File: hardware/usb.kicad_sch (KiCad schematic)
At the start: 7 parts, among them J201 USB_C_Receptacle_USB2.0, U201 SRV05-4

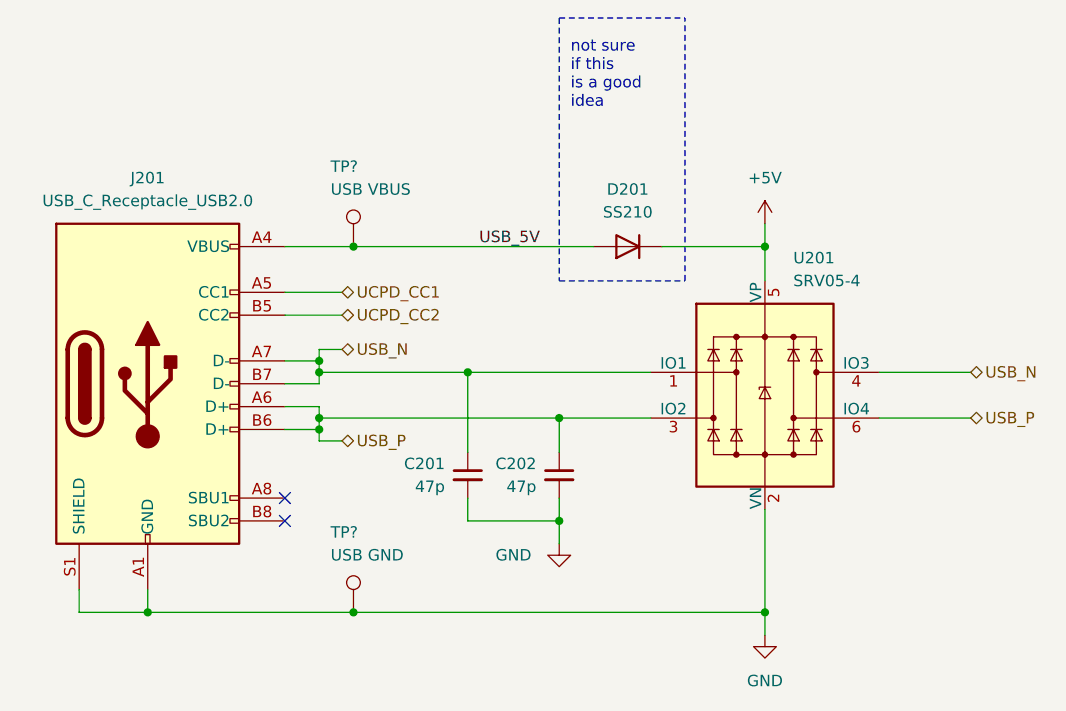
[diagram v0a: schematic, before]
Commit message: finish component selection
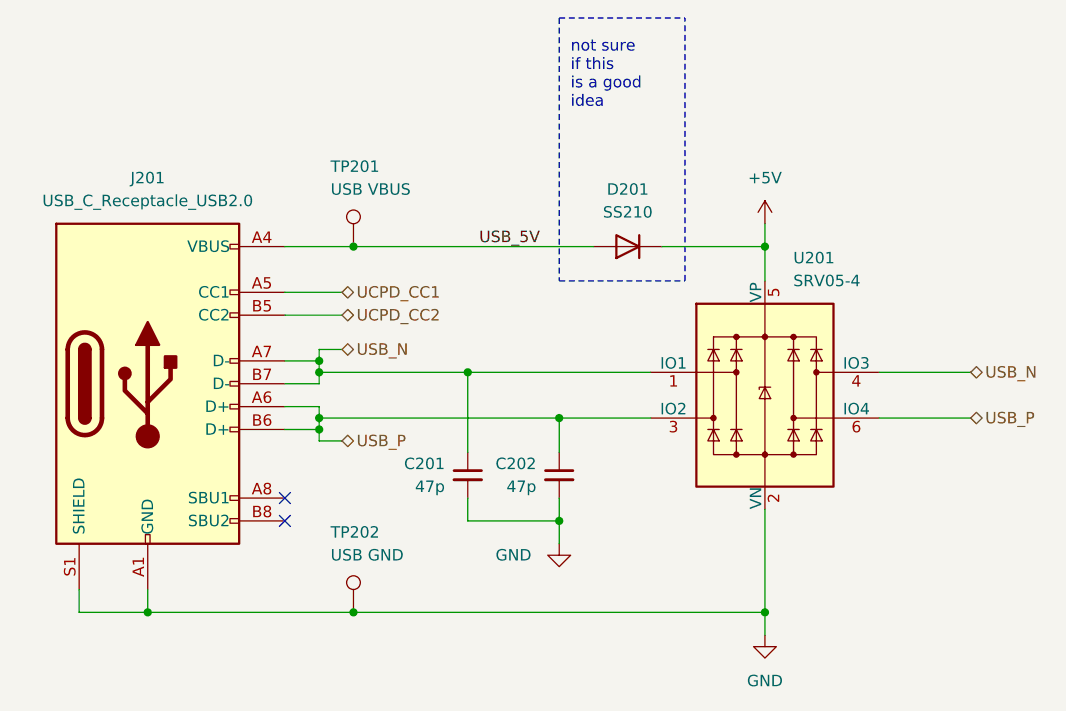
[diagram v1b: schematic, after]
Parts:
- J201: footprint Connector_USB:USB_C_Receptacle_HRO_TYPE-C-31-M-12 -> easyeda2kicad:USB-C-SMD_GT-USB-7052_1; LCSC Part (none) -> C963223
- gave numbers to parts that had none: 2
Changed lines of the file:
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@@
   (title_block
     (title "USB & ESD")
-    (date "2023-06-17")
-    (rev "1.0")
+    (date "2023-10-11")
+    (rev "0.1")
     (company "matei repair lab")
   )
@@
   (symbol (lib_id "Connector:TestPoint") (at 137.16 115.57 0) (unit 1)
     (in_bom yes) (on_board yes) (dnp no)
-    (property "Reference" "TP?" (at 134.62 106.68 0)
+    (property "Reference" "TP202" (at 134.62 106.68 0)
       (effects (font (size 1.27 1.27)) (justify left))
     )
@@
     (pin "1")
     (instances
-      (project "sfoc-stepper"
-        (path "/0306e2fa-4433-4288-91d9-65a3484207ad/3af4e77c-61b4-4c93-bd22-ce60f55b568c"
-          (reference "TP?") (unit 1)
+      (project "lemon-pepper"
+        (path "/0306e2fa-4433-4288-91d9-65a3484207ad/3af4e77c-61b4-4c93-bd22-ce60f55b568c"
+          (reference "TP202") (unit 1)
         )
       )
@@
     (pin "6")
     (instances
-      (project "sfoc-stepper"
+      (project "lemon-pepper"
         (path "/0306e2fa-4433-4288-91d9-65a3484207ad/3af4e77c-61b4-4c93-bd22-ce60f55b568c"
           (reference "U201") (unit 1)
@@
   (symbol (lib_id "Connector:TestPoint") (at 137.16 74.93 0) (unit 1)
     (in_bom yes) (on_board yes) (dnp no)
-    (property "Reference" "TP?" (at 134.62 66.04 0)
+    (property "Reference" "TP201" (at 134.62 66.04 0)
       (effects (font (size 1.27 1.27)) (justify left))
     )
@@
     (pin "1")
     (instances
-      (project "sfoc-stepper"
-        (path "/0306e2fa-4433-4288-91d9-65a3484207ad/3af4e77c-61b4-4c93-bd22-ce60f55b568c"
-          (reference "TP?") (unit 1)
+      (project "lemon-pepper"
+        (path "/0306e2fa-4433-4288-91d9-65a3484207ad/3af4e77c-61b4-4c93-bd22-ce60f55b568c"
+          (reference "TP201") (unit 1)
         )
       )
@@
       (effects (font (size 1.27 1.27)))
     )
-    (property "Footprint" "Connector_USB:USB_C_Receptacle_HRO_TYPE-C-31-M-12" (at 118.11 90.17 0)
+    (property "Footprint" "easyeda2kicad:USB-C-SMD_GT-USB-7052_1" (at 118.11 90.17 0)
       (effects (font (size 1.27 1.27)) hide)
     )
     (property "Datasheet" "https://www.usb.org/sites/default/files/documents/usb_type-c.zip" (at 118.11 90.17 0)
+      (effects (font (size 1.27 1.27)) hide)
+    )
+    (property "LCSC Part" "C963223" (at 114.3 90.17 0)
       (effects (font (size 1.27 1.27)) hide)
     )
@@
     (pin "S1")
     (instances
-      (project "sfoc-stepper"
+      (project "lemon-pepper"
         (path "/0306e2fa-4433-4288-91d9-65a3484207ad/3af4e77c-61b4-4c93-bd22-ce60f55b568c"
           (reference "J201") (unit 1)
@@
     (pin "1")
     (instances
-      (project "sfoc-stepper"
+      (project "lemon-pepper"
         (path "/0306e2fa-4433-4288-91d9-65a3484207ad/3af4e77c-61b4-4c93-bd22-ce60f55b568c"
           (reference "#PWR0202") (unit 1)
@@
     (pin "2")
     (instances
-      (project "sfoc-stepper"
+      (project "lemon-pepper"
         (path "/0306e2fa-4433-4288-91d9-65a3484207ad/3af4e77c-61b4-4c93-bd22-ce60f55b568c"
           (reference "D201") (unit 1)
@@
     (pin "2")
     (instances
-      (project "sfoc-stepper"
+      (project "lemon-pepper"
         (path "/0306e2fa-4433-4288-91d9-65a3484207ad/3af4e77c-61b4-4c93-bd22-ce60f55b568c"
           (reference "C202") (unit 1)
@@
     (pin "1")
     (instances
-      (project "sfoc-stepper"
+      (project "lemon-pepper"
         (path "/0306e2fa-4433-4288-91d9-65a3484207ad/3af4e77c-61b4-4c93-bd22-ce60f55b568c"
           (reference "#PWR0201") (unit 1)
@@
     (pin "2")
     (instances
-      (project "sfoc-stepper"
+      (project "lemon-pepper"
         (path "/0306e2fa-4433-4288-91d9-65a3484207ad/3af4e77c-61b4-4c93-bd22-ce60f55b568c"
           (reference "C201") (unit 1)
@@
     (pin "1")
     (instances
-      (project "sfoc-stepper"
+      (project "lemon-pepper"
         (path "/0306e2fa-4433-4288-91d9-65a3484207ad/3af4e77c-61b4-4c93-bd22-ce60f55b568c"
           (reference "#PWR0203") (unit 1)

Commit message: try new driver
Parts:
- D201: value SS210 -> 1N4148WS; footprint Diode_SMD:D_SMA -> Diode_SMD:D_SOD-323; LCSC Part C14996 -> C2128
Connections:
- net USB_5V: now also U201.5 (VP)
- net USB_N: now also U201.3 (IO2); no longer U201.1 (IO1)
- net USB_P: now also U201.1 (IO1); no longer U201.3 (IO2)
- net +5V renamed Vmot
- net Vmot: no longer U201.5 (VP)
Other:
- note removed: "not sure if this is a good idea"

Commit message: finish layout and prod files
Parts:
- removed TP201: USB VBUS, TestPoint:TestPoint_Pad_D1.0mm, symbol Connector:TestPoint
- removed TP202: USB GND, TestPoint:TestPoint_Pad_D1.0mm, symbol Connector:TestPoint
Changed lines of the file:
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@@
   (junction (at 160.02 93.98) (diameter 0) (color 0 0 0 0)
   )
-  (junction (at 137.16 74.93) (diameter 0) (color 0 0 0 0)
-  )
   (junction (at 160.02 105.41) (diameter 0) (color 0 0 0 0)
-  )
-  (junction (at 137.16 115.57) (diameter 0) (color 0 0 0 0)
   )
   (junction (at 149.86 88.9) (diameter 0) (color 0 0 0 0)
@@
     (stroke (width 0) (type default))
   )
-  (wire (pts (xy 129.54 74.93) (xy 137.16 74.93))
+  (wire (pts (xy 129.54 74.93) (xy 182.88 74.93))
     (stroke (width 0) (type default))
   )
@@
     (stroke (width 0) (type default))
   )
-  (wire (pts (xy 137.16 115.57) (xy 182.88 115.57))
-    (stroke (width 0) (type default))
-  )
   (wire (pts (xy 182.88 74.93) (xy 193.04 74.93))
     (stroke (width 0) (type default))
@@
     (stroke (width 0) (type default))
   )
-  (wire (pts (xy 137.16 74.93) (xy 182.88 74.93))
-    (stroke (width 0) (type default))
-  )
   (wire (pts (xy 195.58 93.98) (xy 199.39 93.98))
     (stroke (width 0) (type default))
@@
     (stroke (width 0) (type default))
   )
-  (wire (pts (xy 114.3 115.57) (xy 137.16 115.57))
+  (wire (pts (xy 114.3 115.57) (xy 182.88 115.57))
     (stroke (width 0) (type default))
   )
@@
     (property "Netclass" "PWR" (at 142.9385 72.39 0)
       (effects (font (size 1.27 1.27) italic) (justify left))
-    )
-  )
-  (symbol (lib_id "Connector:TestPoint") (at 137.16 115.57 0) (unit 1)
-    (in_bom yes) (on_board yes) (dnp no)
-    (property "Reference" "TP202" (at 134.62 106.68 0)
-      (effects (font (size 1.27 1.27)) (justify left))
-    )
-    (property "Value" "USB GND" (at 134.62 109.22 0)
-      (effects (font (size 1.27 1.27)) (justify left))
-    )
-    (property "Footprint" "TestPoint:TestPoint_Pad_D1.0mm" (at 142.24 115.57 0)
-      (effects (font (size 1.27 1.27)) hide)
-    )
-    (property "Datasheet" "~" (at 142.24 115.57 0)
-      (effects (font (size 1.27 1.27)) hide)
-    )
-    (pin "1")
-    (instances
-      (project "lemon-pepper"
-        (path "/0306e2fa-4433-4288-91d9-65a3484207ad/3af4e77c-61b4-4c93-bd22-ce60f55b568c"
-          (reference "TP202") (unit 1)
-        )
-      )
     )
   )
@@
         )
       )
-    )
-  )
-  (symbol (lib_id "Connector:TestPoint") (at 137.16 74.93 0) (unit 1)
-    (in_bom yes) (on_board yes) (dnp no)
-    (property "Reference" "TP201" (at 134.62 66.04 0)
-      (effects (font (size 1.27 1.27)) (justify left))
-    )
-    (property "Value" "USB VBUS" (at 134.62 68.58 0)
-      (effects (font (size 1.27 1.27)) (justify left))
-    )
-    (property "Footprint" "TestPoint:TestPoint_Pad_D1.0mm" (at 142.24 74.93 0)
-      (effects (font (size 1.27 1.27)) hide)
-    )
-    (property "Datasheet" "~" (at 142.24 74.93 0)
-      (effects (font (size 1.27 1.27)) hide)
-    )
-    (pin "1")
-    (instances
-      (project "lemon-pepper"
-        (path "/0306e2fa-4433-4288-91d9-65a3484207ad/3af4e77c-61b4-4c93-bd22-ce60f55b568c"
-          (reference "TP201") (unit 1)
-        )
-      )

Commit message: add readme and update fab files
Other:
- note added: "not sure if good idea"
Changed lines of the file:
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@@
     (stroke (width 0) (type default))
+  )
+  (polyline (pts (xy 205.74 78.74) (xy 205.74 57.15))
+    (stroke (width 0) (type dash))
   )
   (wire (pts (xy 129.54 87.63) (xy 133.35 87.63))
@@
     (stroke (width 0) (type default))
   )
+  (polyline (pts (xy 187.96 57.15) (xy 187.96 78.74))
+    (stroke (width 0) (type dash))
+  )
   (wire (pts (xy 149.86 105.41) (xy 160.02 105.41))
     (stroke (width 0) (type default))
@@
     (stroke (width 0) (type default))
   )
-  (wire (pts (xy 200.66 74.93) (xy 204.47 74.93))
+  (wire (pts (xy 200.66 74.93) (xy 210.82 74.93))
     (stroke (width 0) (type default))
   )
@@
     (stroke (width 0) (type default))
   )
+  (polyline (pts (xy 187.96 57.15) (xy 205.74 57.15))
+    (stroke (width 0) (type dash))
+  )
   (wire (pts (xy 160.02 93.98) (xy 170.18 93.98))
     (stroke (width 0) (type default))
   )
-  (wire (pts (xy 204.47 74.93) (xy 204.47 71.12))
+  (wire (pts (xy 210.82 74.93) (xy 210.82 69.85))
     (stroke (width 0) (type default))
   )
@@
     (stroke (width 0) (type default))
   )
+  (polyline (pts (xy 187.96 78.74) (xy 205.74 78.74))
+    (stroke (width 0) (type dash))
+  )
   (wire (pts (xy 129.54 82.55) (xy 135.89 82.55))
     (stroke (width 0) (type default))
@@
   (wire (pts (xy 133.35 88.9) (xy 149.86 88.9))
     (stroke (width 0) (type default))
+  )
+  (text "not sure if\ngood idea" (at 191.77 63.5 0)
+    (effects (font (size 1.27 1.27)) (justify left bottom))
   )
   (label "USB_5V" (at 151.13 74.93 0) (fields_autoplaced)
@@
     )
   )
-  (symbol (lib_id "matei:Vmot") (at 204.47 71.12 0) (unit 1)
+  (symbol (lib_id "matei:Vmot") (at 210.82 69.85 0) (unit 1)
     (in_bom yes) (on_board yes) (dnp no) (fields_autoplaced)
-    (property "Reference" "#PWR0202" (at 199.39 74.93 0)
-      (effects (font (size 1.27 1.27)) hide)
-    )
-    (property "Value" "Vmot" (at 204.47 66.04 0)
-      (effects (font (size 1.27 1.27)))
-    )
-    (property "Footprint" "" (at 204.47 71.12 0)
-      (effects (font (size 1.27 1.27)) hide)
-    )
-    (property "Datasheet" "" (at 204.47 71.12 0)
-      (effects (font (size 1.27 1.27)) hide)
-    )
+    (property "Reference" "#PWR0202" (at 205.74 73.66 0)
+      (effects (font (size 1.27 1.27)) hide)
+    )
+    (property "Value" "Vmot" (at 210.82 64.77 0)
+      (effects (font (size 1.27 1.27)))
+    )
+    (property "Footprint" "" (at 210.82 69.85 0)
+      (effects (font (size 1.27 1.27)) hide)
+    )
+    (property "Datasheet" "" (at 210.82 69.85 0)
+      (effects (font (size 1.27 1.27)) hide)
+    )

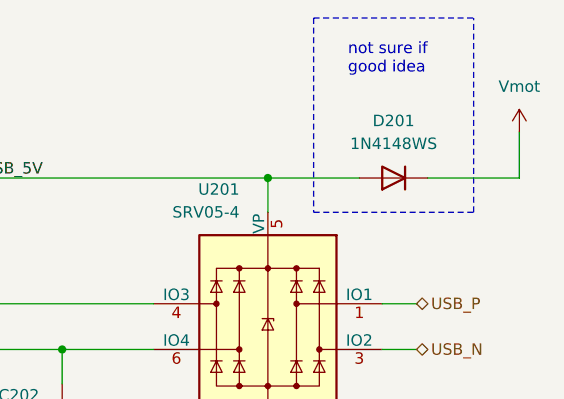
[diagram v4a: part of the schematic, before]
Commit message: start working on current sense
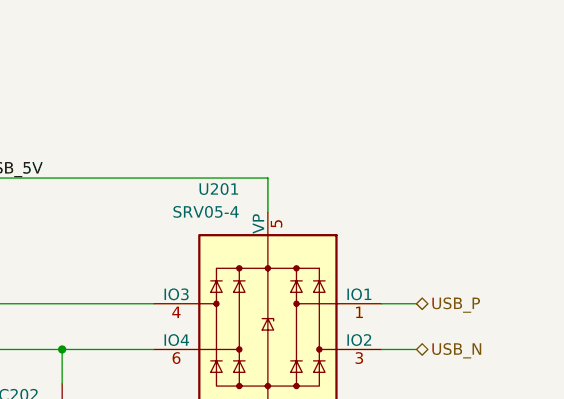
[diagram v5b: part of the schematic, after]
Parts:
- removed D201: 1N4148WS, Diode_SMD:D_SOD-323, symbol Device:D
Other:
- note removed: "not sure if good idea"
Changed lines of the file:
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@@
   (junction (at 182.88 115.57) (diameter 0) (color 0 0 0 0)
-  )
-  (junction (at 182.88 74.93) (diameter 0) (color 0 0 0 0)
   )
   (junction (at 133.35 87.63) (diameter 0) (color 0 0 0 0)
@@
     (stroke (width 0) (type default))
   )
-  (polyline (pts (xy 205.74 78.74) (xy 205.74 57.15))
-    (stroke (width 0) (type dash))
-  )
   (wire (pts (xy 129.54 87.63) (xy 133.35 87.63))
     (stroke (width 0) (type default))
@@
     (stroke (width 0) (type default))
   )
-  (polyline (pts (xy 187.96 57.15) (xy 187.96 78.74))
-    (stroke (width 0) (type dash))
-  )
   (wire (pts (xy 149.86 105.41) (xy 160.02 105.41))
     (stroke (width 0) (type default))
@@
     (stroke (width 0) (type default))
   )
-  (wire (pts (xy 182.88 74.93) (xy 193.04 74.93))
-    (stroke (width 0) (type default))
-  )
   (wire (pts (xy 129.54 80.01) (xy 135.89 80.01))
     (stroke (width 0) (type default))
   )
-  (wire (pts (xy 200.66 74.93) (xy 210.82 74.93))
-    (stroke (width 0) (type default))
-  )
   (wire (pts (xy 160.02 102.87) (xy 160.02 105.41))
     (stroke (width 0) (type default))
@@
     (stroke (width 0) (type default))
   )
-  (polyline (pts (xy 187.96 57.15) (xy 205.74 57.15))
-    (stroke (width 0) (type dash))
-  )
   (wire (pts (xy 160.02 93.98) (xy 170.18 93.98))
     (stroke (width 0) (type default))
   )
-  (wire (pts (xy 210.82 74.93) (xy 210.82 69.85))
-    (stroke (width 0) (type default))
-  )
   (wire (pts (xy 160.02 93.98) (xy 160.02 97.79))
     (stroke (width 0) (type default))
@@
     (stroke (width 0) (type default))
   )
-  (polyline (pts (xy 187.96 78.74) (xy 205.74 78.74))
-    (stroke (width 0) (type dash))
-  )
   (wire (pts (xy 129.54 82.55) (xy 135.89 82.55))
     (stroke (width 0) (type default))
@@
   (wire (pts (xy 133.35 88.9) (xy 149.86 88.9))
     (stroke (width 0) (type default))
-  )
-  (text "not sure if\ngood idea" (at 191.77 63.5 0)
-    (effects (font (size 1.27 1.27)) (justify left bottom))
   )
   (label "USB_5V" (at 151.13 74.93 0) (fields_autoplaced)
@@
         (path "/bcb2c98d-7159-437a-9ffb-b81c5fcc4307/9a7f39aa-afb0-48e5-a983-57776588e1e5"
           (reference "U601") (unit 1)
-        )
-      )
-    )
-  )
-  (symbol (lib_id "Device:D") (at 196.85 74.93 180) (unit 1)
-    (in_bom yes) (on_board yes) (dnp no) (fields_autoplaced)
-    (property "Reference" "D201" (at 196.85 68.58 0)
-      (effects (font (size 1.27 1.27)))
-    )
-    (property "Value" "1N4148WS" (at 196.85 71.12 0)
-      (effects (font (size 1.27 1.27)))
-    )
-    (property "Footprint" "Diode_SMD:D_SOD-323" (at 196.85 74.93 0)
-      (effects (font (size 1.27 1.27)) hide)
-    )
-    (property "Datasheet" "~" (at 196.85 74.93 0)
-      (effects (font (size 1.27 1.27)) hide)
-    )
-    (property "Sim.Device" "D" (at 196.85 74.93 0)
-      (effects (font (size 1.27 1.27)) hide)
-    )
-    (property "Sim.Pins" "1=K 2=A" (at 196.85 74.93 0)
-      (effects (font (size 1.27 1.27)) hide)
-    )
-    (property "LCSC Part" "C2128" (at 196.85 74.93 0)
-      (effects (font (size 1.27 1.27)) hide)
-    )
-    (pin "1")
-    (pin "2")
-    (instances
-      (project "lemon-pepper"
-        (path "/0306e2fa-4433-4288-91d9-65a3484207ad/3af4e77c-61b4-4c93-bd22-ce60f55b568c"
-          (reference "D201") (unit 1)
         )
       )
@@
         )
       )
-    )
-  )
-  (symbol (lib_id "matei:Vmot") (at 210.82 69.85 0) (unit 1)
-    (in_bom yes) (on_board yes) (dnp no) (fields_autoplaced)
-    (property "Reference" "#PWR0202" (at 205.74 73.66 0)
-      (effects (font (size 1.27 1.27)) hide)
-    )
-    (property "Value" "Vmot" (at 210.82 64.77 0)
-      (effects (font (size 1.27 1.27)))
-    )
-    (property "Footprint" "" (at 210.82 69.85 0)
-      (effects (font (size 1.27 1.27)) hide)
-    )
-    (property "Datasheet" "" (at 210.82 69.85 0)
-      (effects (font (size 1.27 1.27)) hide)
-    )
-    (pin "1")
-    (instances
-      (project "lemon-pepper"
-        (path "/0306e2fa-4433-4288-91d9-65a3484207ad/3af4e77c-61b4-4c93-bd22-ce60f55b568c"
-          (reference "#PWR0202") (unit 1)
-        )
-      )

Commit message: work on current sense
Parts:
- J201: footprint easyeda2kicad:USB-C-SMD_GT-USB-7052_1 -> mechanical:usb_c
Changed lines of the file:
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@@
       (effects (font (size 1.27 1.27)))
     )
-    (property "Footprint" "easyeda2kicad:USB-C-SMD_GT-USB-7052_1" (at 118.11 90.17 0)
+    (property "Footprint" "mechanical:usb_c" (at 118.11 90.17 0)
       (effects (font (size 1.27 1.27)) hide)
     )

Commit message: Update BOM field LCSC ID
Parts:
- C201, C202: LCSC ID (none) -> C1567; LCSC Part C1567 -> (none)
- J201: LCSC ID (none) -> C963223; LCSC Part C963223 -> (none)
- U201: LCSC ID (none) -> C7420376; LCSC Part C7420376 -> (none)
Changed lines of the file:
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@@
 			)
 		)
-		(property "LCSC Part" "C7420376"
+		(property "LCSC ID" "C7420376"
 			(at 182.88 91.44 0)
 			(effects
@@
 			)
 		)
-		(property "LCSC Part" "C963223"
+		(property "LCSC ID" "C963223"
 			(at 114.3 90.17 0)
 			(effects
@@
 			)
 		)
-		(property "LCSC Part" "C1567"
+		(property "LCSC ID" "C1567"
 			(at 160.02 100.33 0)
 			(effects
@@
 			)
 		)
-		(property "LCSC Part" "C1567"
+		(property "LCSC ID" "C1567"
 			(at 149.86 100.33 0)
 			(effects
